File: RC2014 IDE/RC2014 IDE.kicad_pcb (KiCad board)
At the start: 2 copper layers, 99.1 x 49.5 mm, 10 parts, among them J1 CONN_02X20, J2 Device power, J4 CONN_01X39, U1 74LS138

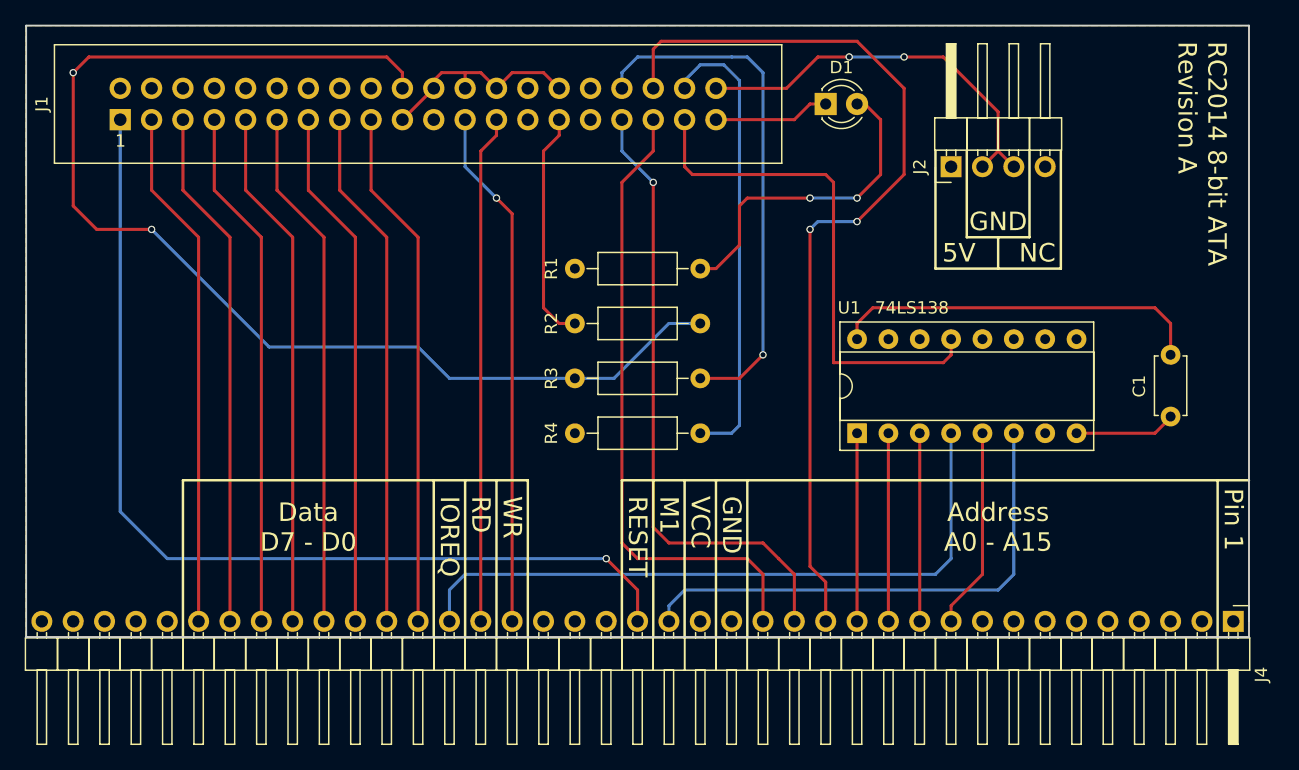
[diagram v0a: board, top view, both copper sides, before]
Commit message: Added OR-gates to R/W signals
Seems other people have been having problems when using RD and WR directly, so adding the OR-gates just in case I need them and can't afford to remake the PCBs.
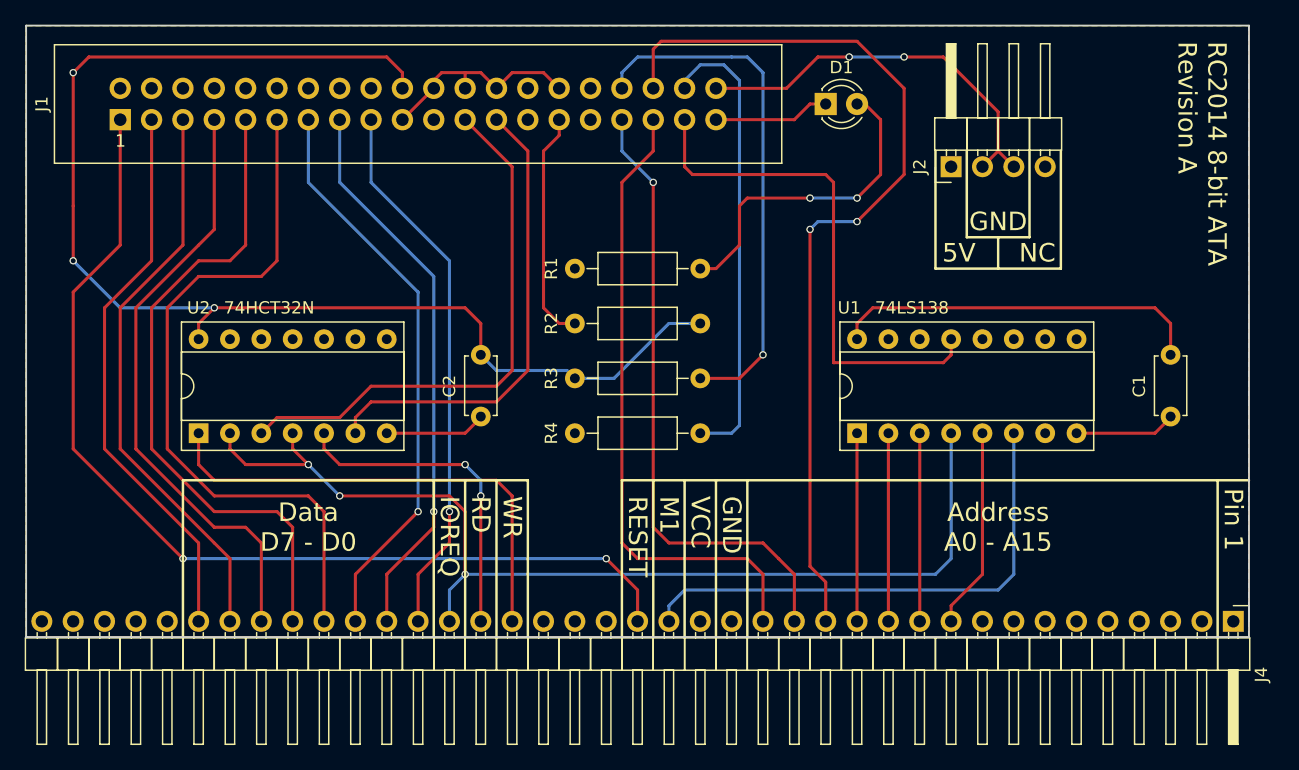
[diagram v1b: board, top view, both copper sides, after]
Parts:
- added C2: 100nF, Capacitors_THT:C_Disc_D4.7mm_W2.5mm_P5.00mm, F.Cu at (153.7, 111.8)
- added U2: 74HCT32N, Housings_DIP:DIP-14_W7.62mm_Socket, F.Cu at (130.8, 118.1)
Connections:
- J1 pad 23: WR -> Net-(IC1-Pad3)
- J1 pad 25: RD -> Net-(IC1-Pad6)
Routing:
- net Net-(IC1-Pad3): track 0.00 -> 44.3 mm
- net Net-(IC1-Pad6): track 0.00 -> 38.2 mm
- net IOREQ: track 54.4 -> 85.0 mm, vias 0 -> 3
- net D3: track 42.2 -> 57.0 mm
- net RD: track 41.2 -> 26.5 mm, vias 0 -> 2
- net D4: track 42.2 -> 53.0 mm
- net GND: track 58.2 -> 66.5 mm
- net VCC: track 128.5 -> 135.6 mm, vias 2 -> 3
- net D5: track 42.2 -> 49.0 mm
- net D2: track 42.2 -> 46.4 mm, vias 0 -> 1
- net D6: track 42.2 -> 46.4 mm
- net D1: track 42.2 -> 45.4 mm, vias 0 -> 1
- net D7: track 42.2 -> 45.4 mm
- net WR: track 42.2 -> 39.2 mm, vias 1 -> 0
- net RESET: track 78.8 -> 81.2 mm, vias 1 -> 2
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
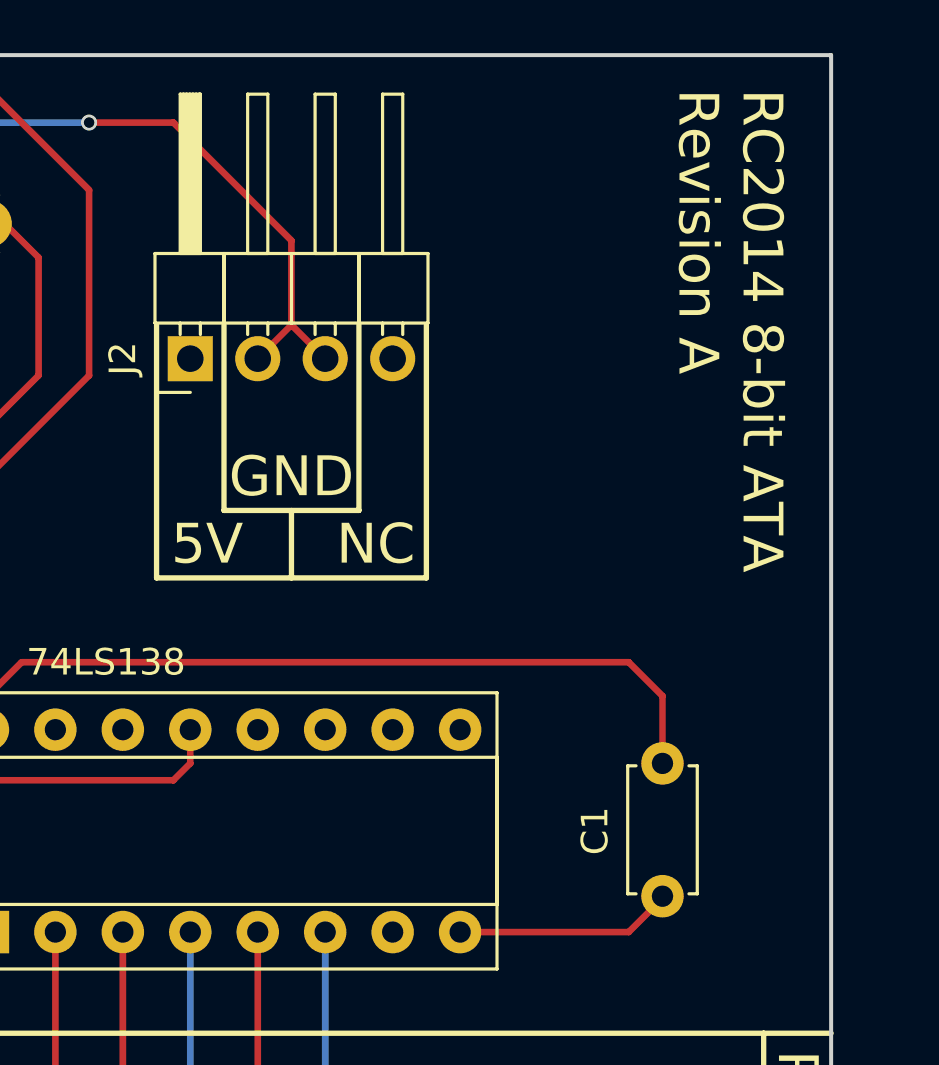
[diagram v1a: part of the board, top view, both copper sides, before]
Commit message: Renumbered ICs to be consistent
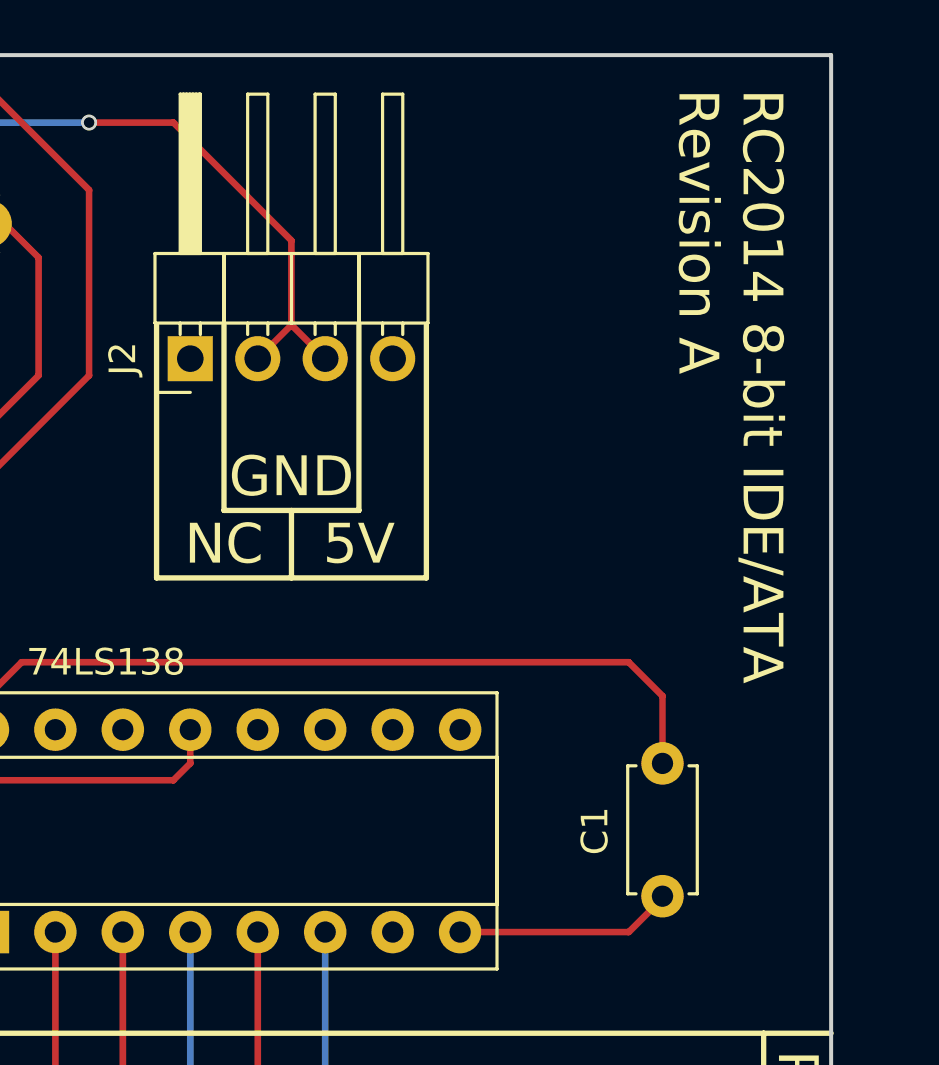
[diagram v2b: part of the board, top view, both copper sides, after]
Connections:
- net Net-(IC1-Pad3) renamed /IOWR
- net Net-(IC1-Pad6) renamed /IORD
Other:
- board text added: "RC2014 8-bit IDE/ATA Revision A"
- board text removed: "RC2014 8-bit ATA Revision A"
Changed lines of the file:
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@@
   (net 27 A2)
   (net 28 "Net-(J1-Pad38)")
-  (net 29 "Net-(IC1-Pad3)")
-  (net 30 "Net-(IC1-Pad6)")
+  (net 29 /IOWR)
+  (net 30 /IORD)
   (net_class Default "This is the default net class."
     (clearance 0.2)
@@
     (uvia_dia 0.3)
     (uvia_drill 0.1)
+    (add_net /IORD)
+    (add_net /IOWR)
     (add_net A0)
     (add_net A1)
@@
     (add_net M1)
     (add_net "Net-(D1-Pad2)")
-    (add_net "Net-(IC1-Pad3)")
-    (add_net "Net-(IC1-Pad6)")
     (add_net "Net-(J1-Pad29)")
     (add_net "Net-(J1-Pad34)")
@@
       (net 2 GND))
     (pad 23 thru_hole oval (at 27.94 0) (size 1.7272 1.7272) (drill 1.016) (layers *.Cu *.Mask)
-      (net 29 "Net-(IC1-Pad3)"))
+      (net 29 /IOWR))
     (pad 24 thru_hole oval (at 27.94 -2.54) (size 1.7272 1.7272) (drill 1.016) (layers *.Cu *.Mask)
       (net 2 GND))
     (pad 25 thru_hole oval (at 30.48 0) (size 1.7272 1.7272) (drill 1.016) (layers *.Cu *.Mask)
-      (net 30 "Net-(IC1-Pad6)"))
+      (net 30 /IORD))
     (pad 26 thru_hole oval (at 30.48 -2.54) (size 1.7272 1.7272) (drill 1.016) (layers *.Cu *.Mask)
       (net 2 GND))
@@
       (net 2 GND))
     (pad 3 thru_hole oval (at 0 5.08 90) (size 1.6 1.6) (drill 0.8) (layers *.Cu *.Mask)
-      (net 29 "Net-(IC1-Pad3)"))
+      (net 29 /IOWR))
     (pad 10 thru_hole oval (at 7.62 10.16 90) (size 1.6 1.6) (drill 0.8) (layers *.Cu *.Mask)
       (net 2 GND))
@@
       (net 2 GND))
     (pad 6 thru_hole oval (at 0 12.7 90) (size 1.6 1.6) (drill 0.8) (layers *.Cu *.Mask)
-      (net 30 "Net-(IC1-Pad6)"))
+      (net 30 /IORD))
     (pad 13 thru_hole oval (at 7.62 2.54 90) (size 1.6 1.6) (drill 0.8) (layers *.Cu *.Mask)
       (net 2 GND))
@@
   (gr_line (start 193.04 102.235) (end 193.04 95.25) (angle 90) (layer F.SilkS) (width 0.2))
   (gr_line (start 198.12 102.235) (end 193.04 102.235) (angle 90) (layer F.SilkS) (width 0.2))
-  (gr_text "RC2014 8-bit ATA\nRevision A" (at 212.09 86.36 270) (layer F.SilkS)
+  (gr_text "RC2014 8-bit IDE/ATA\nRevision A" (at 212.09 86.36 270) (layer F.SilkS)
     (effects (font (size 1.5 1.5) (thickness 0.3)) (justify left))
   )
-  (gr_text NC (at 198.755 103.505) (layer F.SilkS)
+  (gr_text NC (at 193.04 103.505) (layer F.SilkS)
     (effects (font (size 1.5 1.5) (thickness 0.3)))
   )
-  (gr_text 5V (at 192.405 103.505) (layer F.SilkS)
+  (gr_text 5V (at 198.12 103.505) (layer F.SilkS)
     (effects (font (size 1.5 1.5) (thickness 0.3)))
   )
@@
   (gr_line (start 215.9 134.62) (end 215.9 85.09) (angle 90) (layer Edge.Cuts) (width 0.15))
   (gr_line (start 116.84 134.62) (end 215.9 134.62) (angle 90) (layer Edge.Cuts) (width 0.15))
-  (segment (start 153.67 111.76) (end 154.94 113.03) (width 0.25) (layer B.Cu) (net 1) (status 400000))
-  (segment (start 160.655 113.03) (end 161.29 113.665) (width 0.25) (layer B.Cu) (net 1) (status 800000))
+  (segment (start 153.67 111.76) (end 154.94 113.03) (width 0.25) (layer B.Cu) (net 1))
+  (segment (start 160.655 113.03) (end 161.29 113.665) (width 0.25) (layer B.Cu) (net 1))
   (segment (start 154.94 113.03) (end 160.655 113.03) (width 0.25) (layer B.Cu) (net 1))
   (segment (start 120.65 104.14) (end 121.92 105.41) (width 0.25) (layer B.Cu) (net 1))
